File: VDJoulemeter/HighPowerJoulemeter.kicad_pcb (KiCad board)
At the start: 4 copper layers, 119.2 x 118.6 mm, 92 parts, among them J1 XT60-M, J2 XT60-M, J3 22035035, J4 22035035, U3 MCP2562, U4 TMCS1126B6AQDVGRQ1, U5 MCP6286T-E/OT, U6 PTPSM365R6V5RDNR, U8 ADS1118QDGSRQ1, U9 MIC5219-3.3YM5-TR

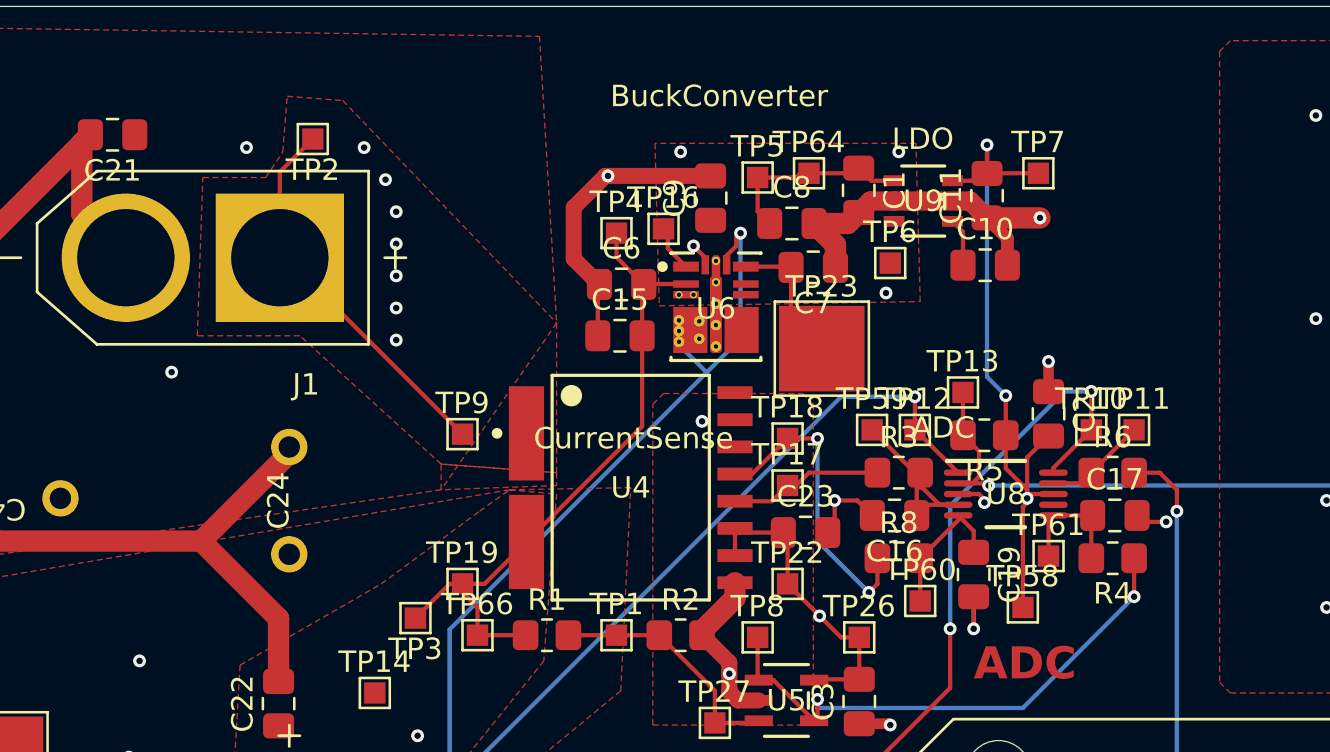
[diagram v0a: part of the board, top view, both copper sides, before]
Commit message: minor courtyard moves
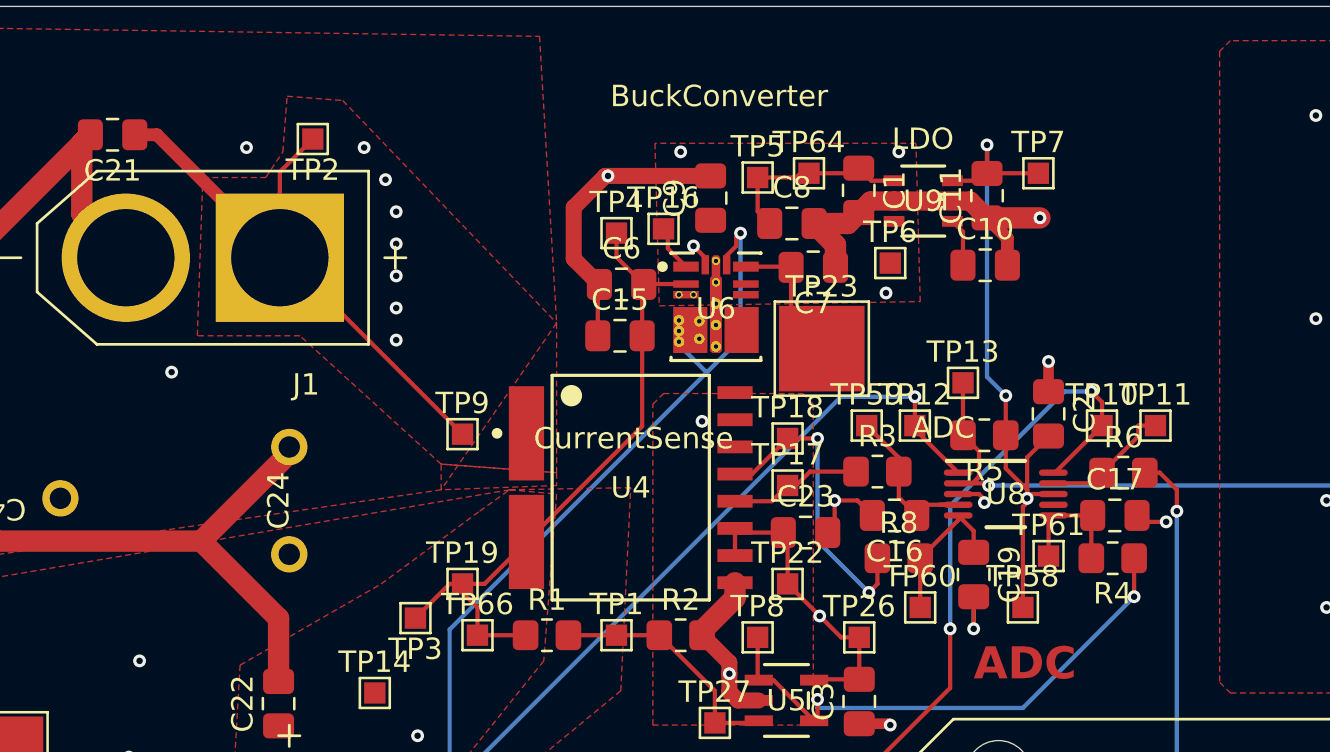
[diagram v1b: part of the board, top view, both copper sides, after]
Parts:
- moved TP11 1.02 mm to (157.0, -665.0)
- moved R3 1.00 mm to (144.0, -662.9)
- moved TP10 0.54 mm to (154.5, -665.0)
- moved R6 0.50 mm to (155.5, -662.8)
- moved TP13 0.45 mm to (148.0, -667.0)
- moved TP59 0.32 mm to (143.5, -665.0)
- moved TP60 0.30 mm to (146.0, -656.5)
- moved TP12 0.20 mm to (145.8, -665.0)
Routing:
- net 48V_IN: track 18.3 -> 27.5 mm
- net Net-(U8-AIN0): track 10.7 -> 8.19 mm
- net Net-(U8-DOUT_DRDY_N): track 4.81 -> 6.19 mm
- net /I_Sense: track 7.21 -> 6.23 mm
- net /STM_MISO: track 69.0 -> 68.5 mm
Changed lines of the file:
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@@
 	(footprint "TestPoint:TestPoint_Pad_1.0x1.0mm"
 		(layer "F.Cu")
-		(at 156 -664.8)
+		(at 157 -665)
 		(descr "SMD rectangular pad as test Point, square 1.0mm side length")
 		(tags "test point SMD pad rectangle square")
@@
 	(footprint "Resistor_SMD:R_0805_2012Metric_Pad1.20x1.40mm_HandSolder"
 		(layer "F.Cu")
-		(at 145 -662.8)
+		(at 144 -662.85)
 		(descr "Resistor SMD 0805 (2012 Metric), square (rectangular) end terminal, IPC-7351 nominal with elongated pad for handsoldering. (Body size source: IPC-SM-782 page 72, https://www.pcb-3d.com/wordpress/wp-content/uploads/ipc-sm-782a_amendment_1_and_2.pdf), generated with kicad-footprint-generator")
 		(tags "resistor handsolder")
@@
 	(footprint "Resistor_SMD:R_0805_2012Metric_Pad1.20x1.40mm_HandSolder"
 		(layer "F.Cu")
-		(at 155 -662.8)
+		(at 155.5 -662.8)
 		(descr "Resistor SMD 0805 (2012 Metric), square (rectangular) end terminal, IPC-7351 nominal with elongated pad for handsoldering. (Body size source: IPC-SM-782 page 72, https://www.pcb-3d.com/wordpress/wp-content/uploads/ipc-sm-782a_amendment_1_and_2.pdf), generated with kicad-footprint-generator")
 		(tags "resistor handsolder")
@@
 	(footprint "TestPoint:TestPoint_Pad_1.0x1.0mm"
 		(layer "F.Cu")
-		(at 146 -656.8)
+		(at 146 -656.5)
 		(descr "SMD rectangular pad as test Point, square 1.0mm side length")
 		(tags "test point SMD pad rectangle square")
@@
 	(footprint "TestPoint:TestPoint_Pad_1.0x1.0mm"
 		(layer "F.Cu")
-		(at 143.75 -664.8)
+		(at 143.5 -665)
 		(descr "SMD rectangular pad as test Point, square 1.0mm side length")
 		(tags "test point SMD pad rectangle square")
@@
 	(footprint "TestPoint:TestPoint_Pad_1.0x1.0mm"
 		(layer "F.Cu")
-		(at 145.75 -664.8)
+		(at 145.75 -665)
 		(descr "SMD rectangular pad as test Point, square 1.0mm side length")
 		(tags "test point SMD pad rectangle square")
@@
 	(footprint "TestPoint:TestPoint_Pad_1.0x1.0mm"
 		(layer "F.Cu")
-		(at 148 -666.55)
+		(at 148 -667)
 		(descr "SMD rectangular pad as test Point, square 1.0mm side length")
 		(tags "test point SMD pad rectangle square")
@@
 	(footprint "TestPoint:TestPoint_Pad_1.0x1.0mm"
 		(layer "F.Cu")
-		(at 154 -664.8)
+		(at 154.5 -665)
 		(descr "SMD rectangular pad as test Point, square 1.0mm side length")
 		(tags "test point SMD pad rectangle square")
@@
 	)
 	(segment
-		(start 146 -662.200002)
-		(end 146 -662.8)
-		(width 0.2)
-		(layer "F.Cu")
-		(net 6)
-	)
-	(segment
 		(start 147.775001 -661.300001)
 		(end 146.900001 -661.300001)
@@
 	)
 	(segment
-		(start 145.8375 -660.8)
-		(end 145.8375 -662.6375)
-		(width 0.2)
-		(layer "F.Cu")
-		(net 6)
-	)
-	(segment
-		(start 145.8375 -662.6375)
-		(end 146 -662.8)
-		(width 0.2)
-		(layer "F.Cu")
-		(net 6)
-	)
-	(segment
 		(start 146.337501 -661.300001)
 		(end 145.8375 -660.8)
@@
 	)
 	(segment
-		(start 146 -662.8)
-		(end 146 -662.1)
+		(start 143.5 -665)
+		(end 145 -663.5)
 		(width 0.2)
 		(layer "F.Cu")
@@
 	)
 	(segment
-		(start 145.75 -662.8)
-		(end 146 -662.8)
+		(start 145 -661.6375)
+		(end 145.8375 -660.8)
 		(width 0.2)
 		(layer "F.Cu")
@@
 	)
 	(segment
-		(start 146.900001 -661.300001)
-		(end 146 -662.200002)
+		(start 145 -662.85)
+		(end 145 -661.6375)
 		(width 0.2)
 		(layer "F.Cu")
@@
 	)
 	(segment
-		(start 143.75 -664.8)
-		(end 145.75 -662.8)
+		(start 145 -663.5)
+		(end 145 -662.85)
 		(width 0.2)
 		(layer "F.Cu")
@@
 	)
 	(segment
-		(start 146 -659.024998)
-		(end 146 -656.8)
-		(width 0.2)
-		(layer "F.Cu")
-		(net 8)
-	)
-	(segment
 		(start 148.5 -660.075)
 		(end 147.775001 -660.799999)
@@
 	)
 	(segment
+		(start 146 -656.5)
+		(end 146 -658.8)
+		(width 0.2)
+		(layer "F.Cu")
+		(net 8)
+	)
+	(segment
 		(start 146 -658.8)
 		(end 147.775001 -660.575001)
@@
 	)
 	(segment
+		(start 110.30825 -678.6)
+		(end 116.05825 -672.85)
+		(width 0.6)
+		(layer "F.Cu")
+		(net 9)
+	)
+	(segment
+		(start 109.275 -678.6)
+		(end 110.30825 -678.6)
+		(width 0.6)
+		(layer "F.Cu")
+		(net 9)
+	)
+	(segment
 		(start 116.35 -672.85)
 		(end 124.6 -664.6)
@@
 	)
 	(segment
-		(start 140.8 -662.8)
-		(end 144 -662.8)
+		(start 140.2 -662.2)
+		(end 139.8 -662.2)
 		(width 0.2)
 		(layer "F.Cu")
@@
 	)
 	(segment
-		(start 140.2 -662.2)
-		(end 140.8 -662.8)
+		(start 139.065001 -661.465001)
+		(end 139.8 -662.2)
 		(width 0.2)
 		(layer "F.Cu")
@@
 	)
 	(segment
-		(start 139.8 -662.2)
+		(start 140.85 -662.85)
 		(end 140.2 -662.2)
 		(width 0.2)
@@
 	)
 	(segment
-		(start 139.065001 -661.465001)
-		(end 139.8 -662.2)
+		(start 137.340249 -661.465001)
+		(end 139.065001 -661.465001)
 		(width 0.2)
 		(layer "F.Cu")
@@
 	)
 	(segment
-		(start 137.340249 -661.465001)
-		(end 139.065001 -661.465001)
+		(start 143 -662.85)
+		(end 140.85 -662.85)
 		(width 0.2)
 		(layer "F.Cu")
@@
 	)
 	(segment
+		(start 148 -664.55)
+		(end 148 -667)
+		(width 0.2)
+		(layer "F.Cu")
+		(net 13)
+	)
+	(segment
 		(start 147.775001 -662.300002)
 		(end 148.437812 -662.300002)
@@
 	)
 	(segment
-		(start 148 -666.55)
-		(end 148 -664.55)
-		(width 0.2)
-		(layer "F.Cu")
-		(net 13)
-	)
-	(segment
 		(start 148.437812 -662.300002)
 		(end 148.751001 -662.613191)
@@
 	)
 	(segment
-		(start 152.225002 -662.300002)
-		(end 153.500002 -662.300002)
+		(start 154.5 -662.8)
+		(end 156.2 -664.5)
+		(width 0.2)
+		(layer "F.Cu")
+		(net 14)
+	)
+	(segment
+		(start 156.2 -664.5)
+		(end 156.2 -665)
 		(width 0.2)
 		(layer "F.Cu")
@@
 	)
 	(segment
-		(start 154 -662.8)
-		(end 156 -664.8)
+		(start 154.000002 -662.300002)
+		(end 154.5 -662.8)
 		(width 0.2)
 		(layer "F.Cu")
@@
 	)
 	(segment
-		(start 153.500002 -662.300002)
-		(end 154 -662.8)
+		(start 152.225002 -662.300002)
+		(end 154.000002 -662.300002)
 		(width 0.2)
 		(layer "F.Cu")
@@
 	)
 	(segment
-		(start 156 -662.8)
-		(end 157.2 -662.8)
+		(start 157 -665)
+		(end 156.2 -665)
 		(width 0.2)
 		(layer "F.Cu")
-		(net 15)
+		(net 14)
 	)
 	(segment
@@
 	)
 	(segment
+		(start 157.2 -662.8)
+		(end 156.5 -662.8)
+		(width 0.2)
+		(layer "F.Cu")
+		(net 15)
+	)
+	(segment
 		(start 121.946 -616.821)
 		(end 121.8 -616.675)
@@
 	)
 	(segment
-		(start 152.225002 -663.025002)
-		(end 154 -664.8)
-		(width 0.2)
-		(layer "F.Cu")
-		(net 17)
-	)
-	(segment
 		(start 129.089 -640.089)
 		(end 129.781552 -640.089)
@@
 	)
 	(segment
-		(start 152.225002 -662.800001)
-		(end 152.225002 -663.025002)
-		(width 0.2)
-		(layer "F.Cu")
-		(net 17)
-	)
-	(segment
 		(start 147.4 -652.735268)
 		(end 147.4 -655.5)
@@
 	)
 	(segment
-		(start 154 -664.8)
-		(end 154 -666.6)
+		(start 127.241552 -637.549)
+		(end 127.866 -638.173448)
 		(width 0.2)
 		(layer "F.Cu")
@@
 	)
 	(segment
-		(start 127.241552 -637.549)
-		(end 127.866 -638.173448)
+		(start 154.5 -665)
+		(end 154.5 -666.1)
 		(width 0.2)
 		(layer "F.Cu")
@@
 		(net 17)
 	)
+	(segment
+		(start 154.5 -666.1)
+		(end 154 -666.6)
+		(width 0.2)
+		(layer "F.Cu")
+		(net 17)
+	)
+	(segment
+		(start 152.300001 -662.800001)
+		(end 152.225002 -662.800001)
+		(width 0.2)
+		(layer "F.Cu")
+		(net 17)
+	)
+	(segment
+		(start 154.5 -665)
+		(end 152.300001 -662.800001)
+		(width 0.2)
+		(layer "F.Cu")
+		(net 17)
+	)
 	(via
 		(at 154 -666.6)
@@
 	)
 	(segment
-		(start 118.275 -611.275)
-		(end 118.2 -611.2)
-		(width 0.2)
-		(layer "F.Cu")
-		(net 19)
-	)
-	(segment
-		(start 145.75 -664.8)
-		(end 145.75 -664.55)
+		(start 145.75 -665)
+		(end 145.75 -664.825002)
 		(width 0.2)
 		(layer "F.Cu")
@@
 	)
 	(segment
-		(start 145.75 -664.55)
-		(end 146.025002 -664.55)
+		(start 145.75 -664.825002)
+		(end 147.775001 -662.800001)
 		(width 0.2)
 		(layer "F.Cu")
@@
 	)
 	(segment
-		(start 120.2 -611.275)
-		(end 118.275 -611.275)
+		(start 145.75 -665)
+		(end 145.75 -666.35)
 		(width 0.2)
 		(layer "F.Cu")
@@
 	)
 	(segment
-		(start 146.025002 -664.55)
-		(end 147.775001 -662.800001)
+		(start 118.275 -611.275)
+		(end 118.2 -611.2)
 		(width 0.2)
 		(layer "F.Cu")
@@
 	)
 	(segment
-		(start 145.75 -664.8)
-		(end 145.75 -666.35)
+		(start 120.2 -611.275)
+		(end 118.275 -611.275)
 		(width 0.2)
 		(layer "F.Cu")
